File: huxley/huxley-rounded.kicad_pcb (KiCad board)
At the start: 4 copper layers, 124 x 124 mm, 165 parts, among them J1 CT3151V1-2, J11 SMA_RF2-04A-T-00-50-G, J13 SMA_RF2-04A-T-00-50-G, J15 SMA_RF2-04A-T-00-50-G, J17 SMA_RF2-04A-T-00-50-G, J18 SMA_RF2-04A-T-00-50-G, J19 SMA_RF2-04A-T-00-50-G, J2 CT3151V1-2, J20 SMA_RF2-04A-T-00-50-G, J21 61300211121, J22 SMA_RF2-04A-T-00-50-G, J24 CT3151V1-2, J25 61300211121, J26 61300211121, J27 61300211121, J28 61300211121, J29 61300211121, J3 CT3151V1-2, J30 61300211121, J31 61300211121, J32 61300211121, J34 CT3151V1-0, J35 CT3151V1-2, J37 CT3151V1-0, J39 CT3151V1-2, J4 SMA_RF2-04A-T-00-50-G, J5 SMA_RF2-04A-T-00-50-G, J7 SMA_RF2-04A-T-00-50-G, J9 SMA_RF2-04A-T-00-50-G, U2 LM134H, U3 21-0036K_MXM, U4 TMUX1112PWR, U5 TMUX1112PWR, U6 NVT2010PW_118

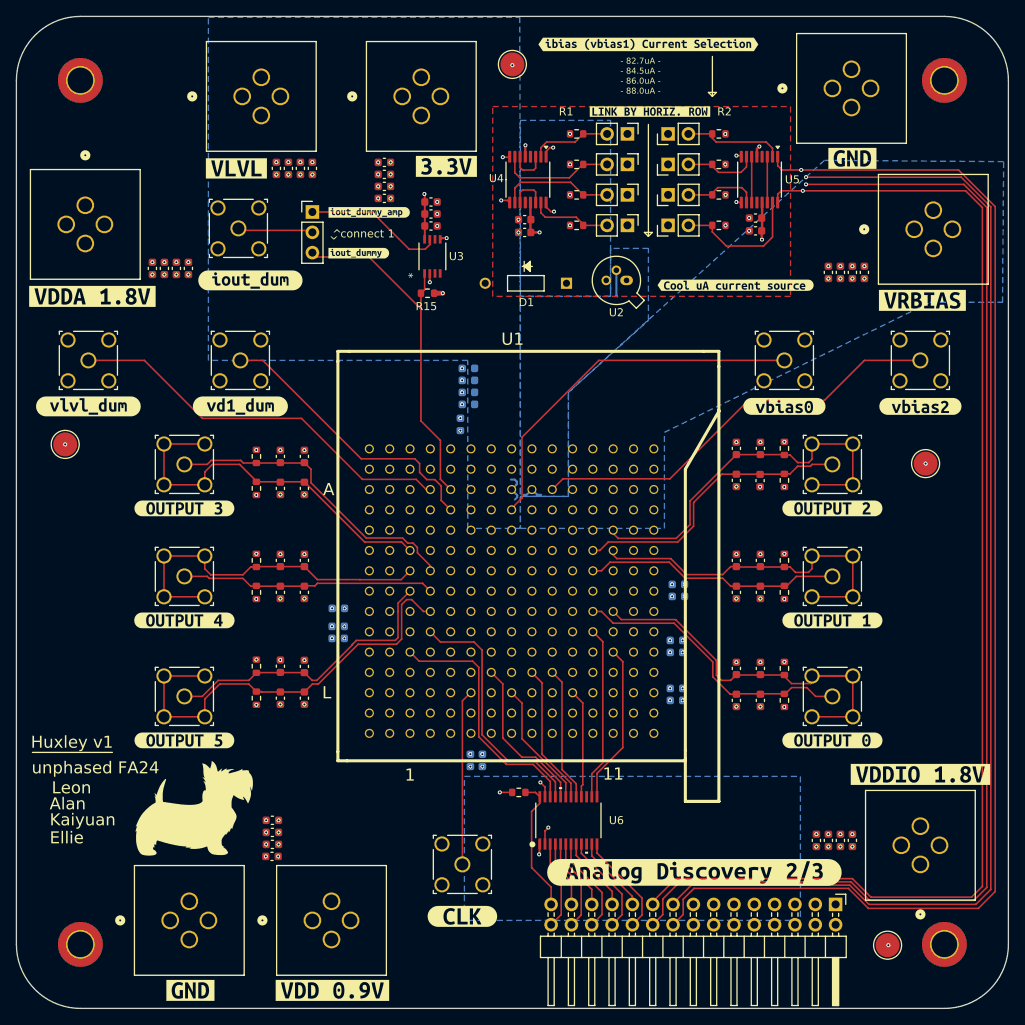
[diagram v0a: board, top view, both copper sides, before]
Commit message: added DNP prop to some caps and updated bom; added regular and rounded board outputs
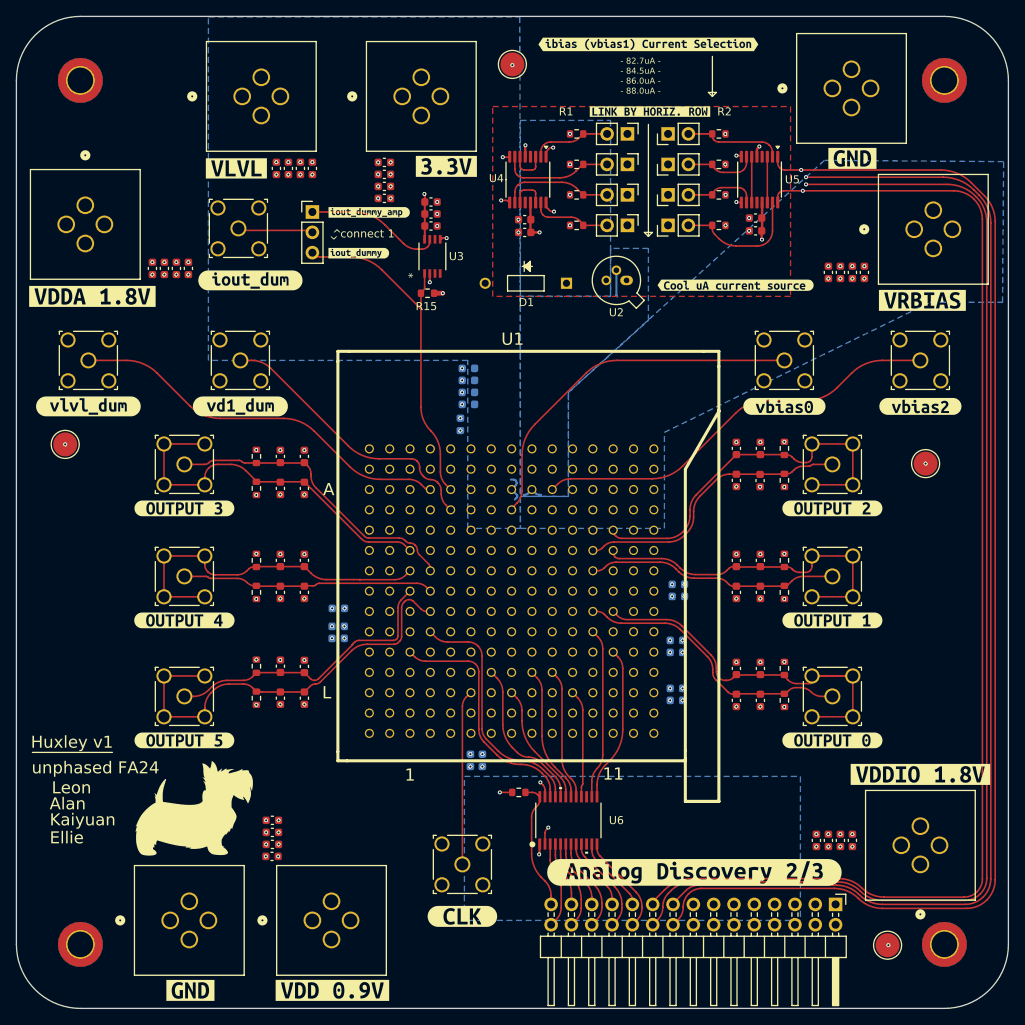
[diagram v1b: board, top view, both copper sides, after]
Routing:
- net IBIAS_SEL1: track 195.1 -> 193.0 mm
- net IBIAS_SEL4: track 190.7 -> 189.0 mm
- net IBIAS_SEL3: track 199.8 -> 198.1 mm
- net IBIAS_SEL2: track 197.2 -> 195.7 mm
- net vlvl_p_dummy: track 49.4 -> 48.2 mm
- net vbias2: track 52.7 -> 51.5 mm
- net iout_dummy: track 45.2 -> 44.3 mm
- net vd1_dummy: track 35.7 -> 34.9 mm
- net TSCAN_EN: track 31.5 -> 30.6 mm
- net output_0-: track 46.6 -> 45.7 mm
- net TSCAN_OUT: track 31.2 -> 30.4 mm
- net output_5-: track 54.9 -> 54.0 mm
- net output_2+: track 36.1 -> 35.3 mm
- net output_0+: track 36.1 -> 35.3 mm
- net output_2-: track 49.4 -> 48.7 mm
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
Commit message: updated huxley-rounded to v1.1
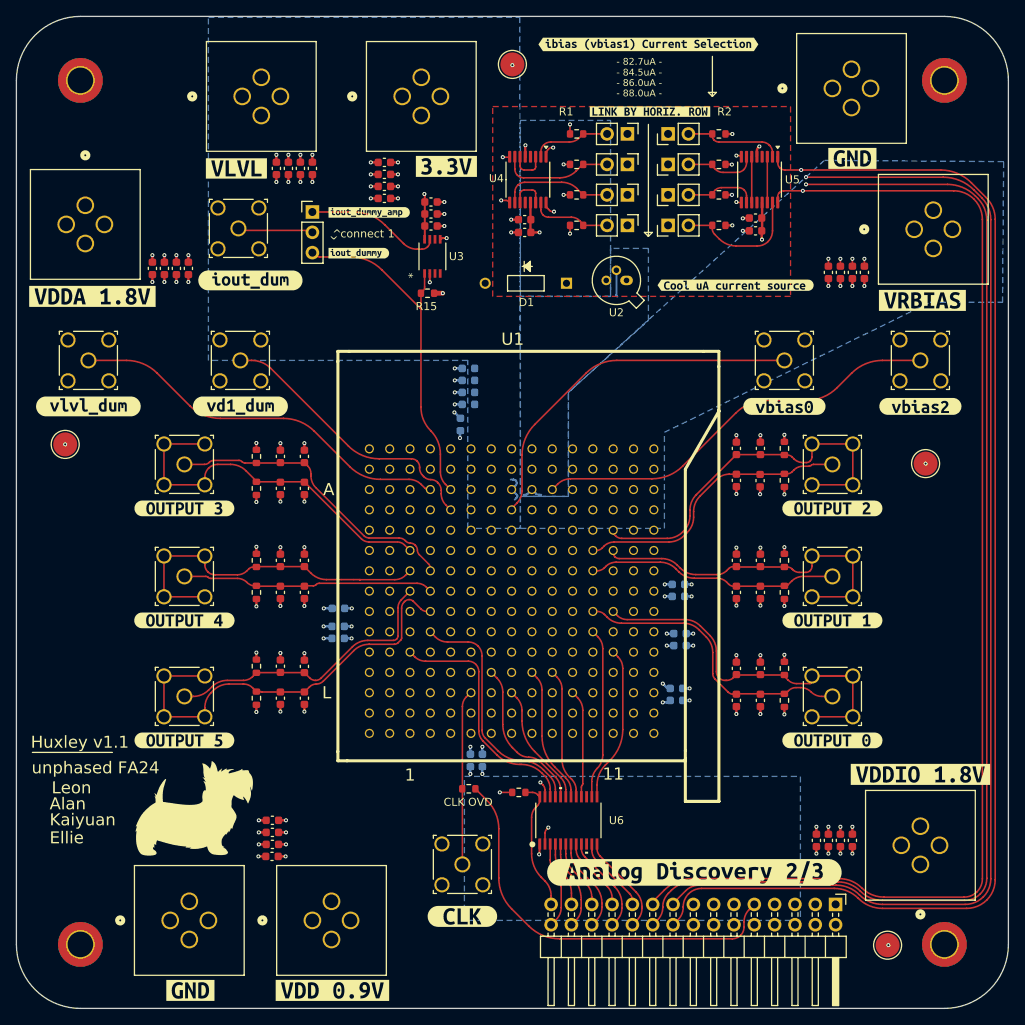
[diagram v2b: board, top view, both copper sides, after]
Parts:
- added R32: R, Resistor_SMD:R_0603_1608Metric, F.Cu at (99.5, 141.6)
- U3: value 21-0036K_MXM -> MAX40201FAUA+
- moved C46 0.96 mm to (126.0, 123.7)
- moved C47 0.96 mm to (126.0, 122.2)
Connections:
- J6 pad 1: unconnected-(J6B-Scope_Ch1+-Pad1) -> scope_ch1+
- J6 pad 2: unconnected-(J6B-Scope_Ch1--Pad2) -> scope_ch1-
- J6 pad 3: unconnected-(J6B-Scope_Ch2+-Pad3) -> scope_ch2+
- J6 pad 4: unconnected-(J6B-Scope_Ch2--Pad4) -> scope_ch2-
- J6 pad 9: unconnected-(J6C-WaveformGen1-Pad9) -> Net-(J6C-WaveformGen1)
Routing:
- net GND: track 7.87 -> 86.1 mm
- net Net-(J6C-WaveformGen1): track 0.00 -> 50.8 mm
- net PP_VDDIO_1V8: track 1.99 -> 9.70 mm
- net PP_VDD_0V9: track 0.00 -> 7.25 mm
- net PP_TAVDD_1V8: track 3.40 -> 10.6 mm
- net /ibias/ibias_m: track 0.00 -> 3.83 mm
- net vlvl: track 3.49 -> 7.19 mm
- net vrbias: track 0.00 -> 3.70 mm
- net PP_SYS_3V3: track 15.2 -> 18.9 mm
- net output_0+: track 35.3 -> 36.7 mm
- net output_0-: track 45.7 -> 47.0 mm
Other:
- board text added: "CLK OVD"
- board text added: "Huxley v1.1"
- board text removed: "Huxley v1"
